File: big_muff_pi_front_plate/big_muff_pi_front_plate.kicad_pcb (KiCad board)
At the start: 2 copper layers, 80 x 100 mm, 13 parts, among them J1 top_panel_connector

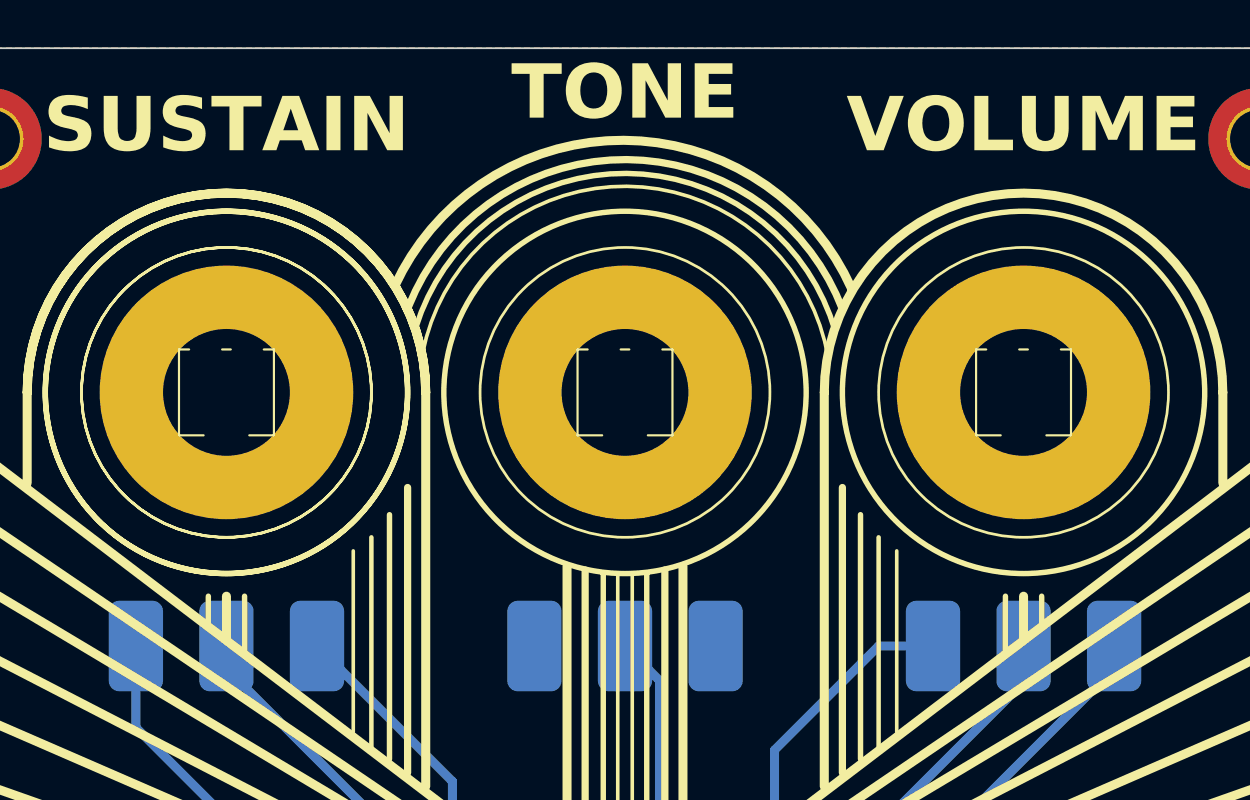
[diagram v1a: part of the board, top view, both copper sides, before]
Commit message: Pots rotated, more space for the battery.
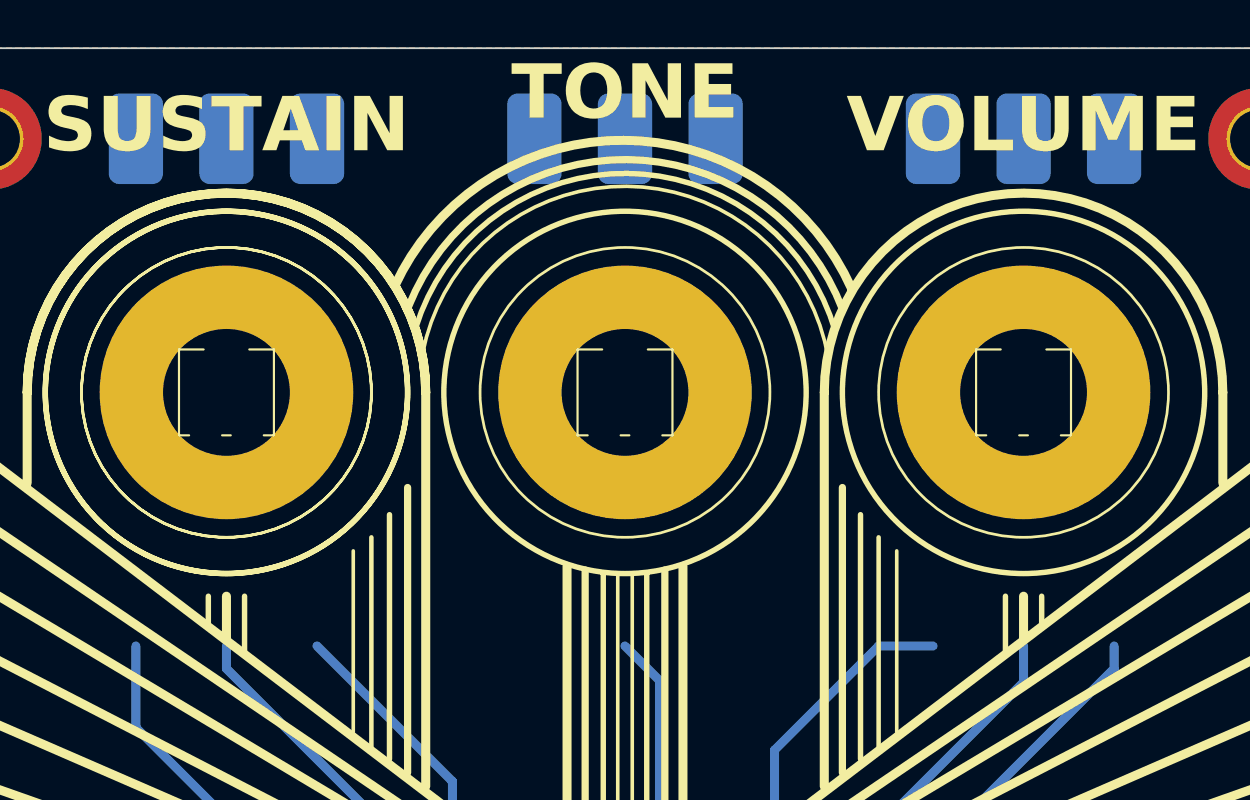
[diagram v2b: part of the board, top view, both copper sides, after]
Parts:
- turned RV1 to 180 degrees
- turned RV2 to 180 degrees
- turned RV3 to 180 degrees

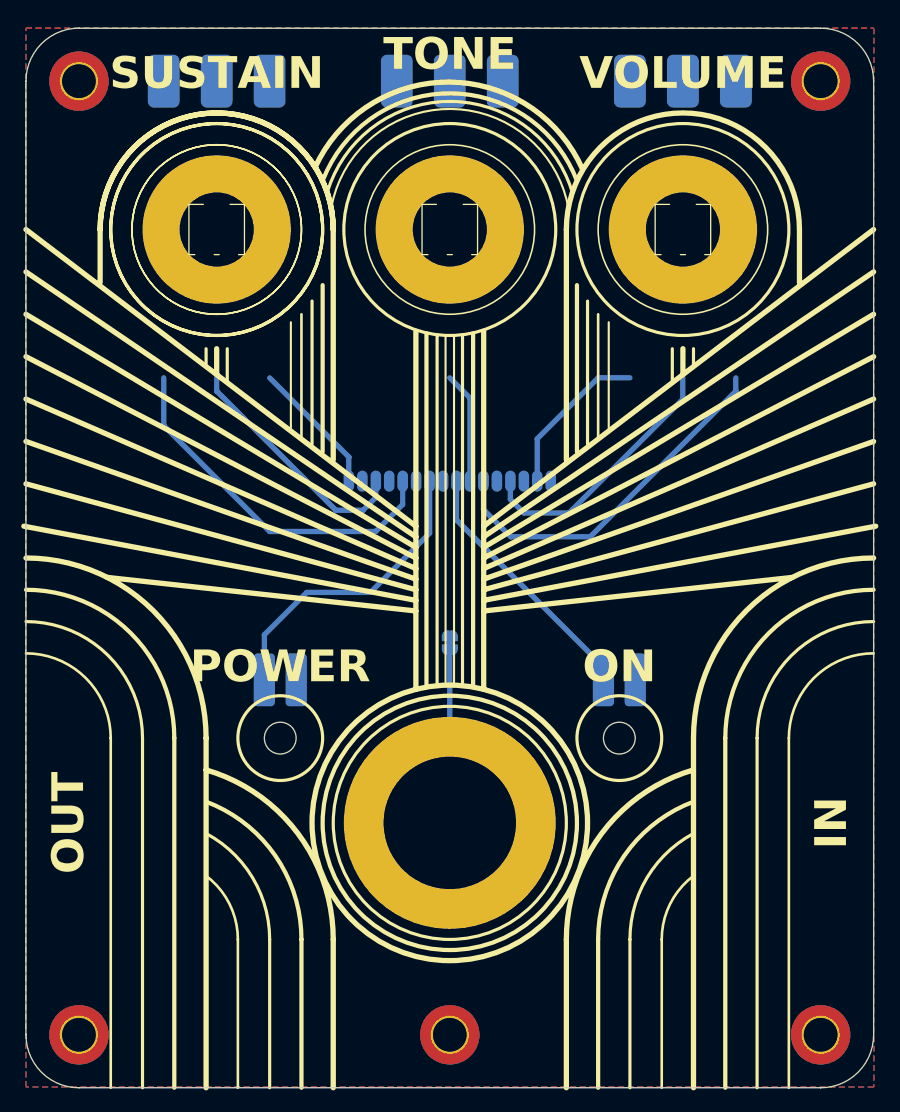
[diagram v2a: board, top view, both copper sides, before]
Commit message: Potentiometers checked, LED updated
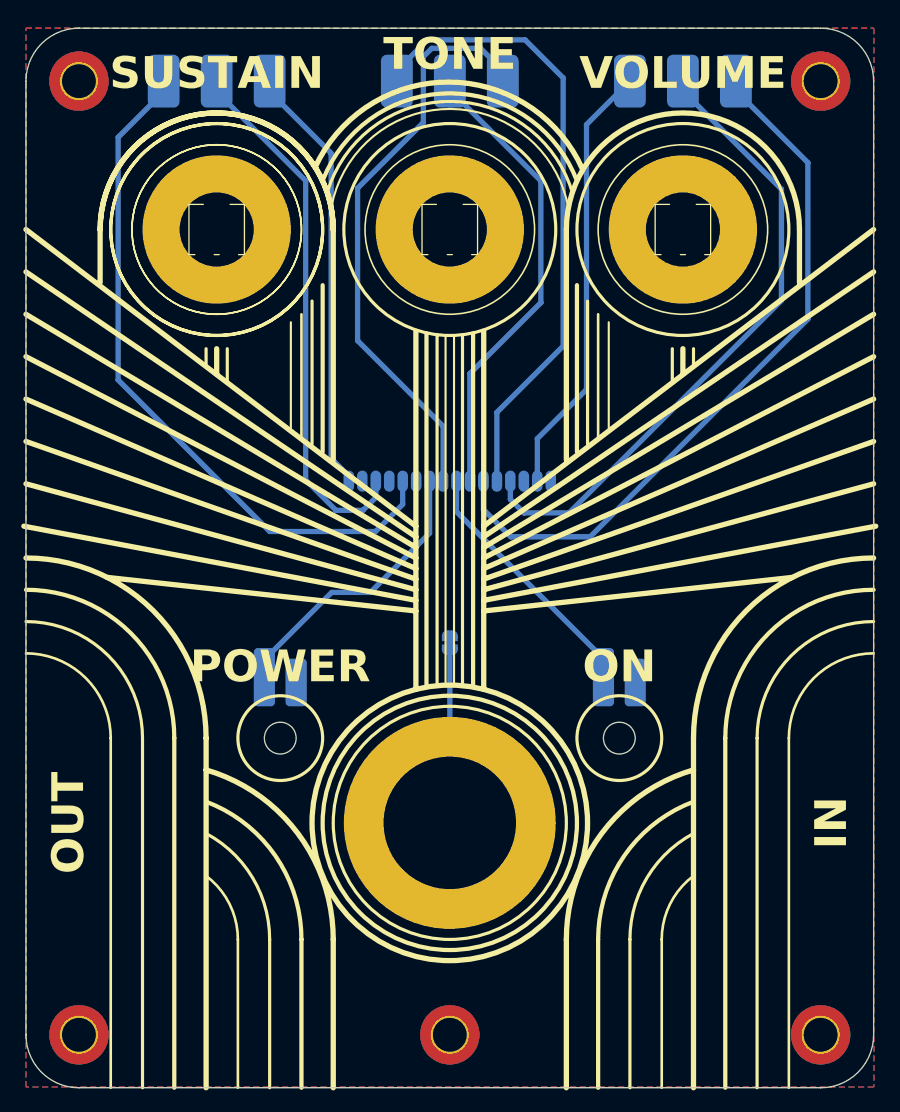
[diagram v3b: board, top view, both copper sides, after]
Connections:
- J1 pad 1: unconnected-(J1F-VCC-Pad1) -> 9V
- J1 pad 3: unconnected-(J1F-GND-Pad3) -> 0
- RV1 pad 1: Net-(J1A-Pin_2) -> Net-(J1A-Pin_6)
- RV1 pad 3: Net-(J1A-Pin_6) -> Net-(J1A-Pin_2)
- RV2 pad 1: Net-(J1B-Pin_5) -> Net-(J1B-Pin_9)
- RV2 pad 3: Net-(J1B-Pin_9) -> Net-(J1B-Pin_5)
- RV3 pad 1: Net-(J1C-Pin_12) -> Net-(J1C-Pin_16)
- RV3 pad 3: Net-(J1C-Pin_16) -> Net-(J1C-Pin_12)
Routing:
- net Net-(J1B-Pin_5): track 0.00 -> 60.0 mm
- net Net-(J1B-Pin_9): track 0.00 -> 55.7 mm
- net Net-(J1A-Pin_4): track 25.0 -> 60.7 mm
- net Net-(J1A-Pin_6): track 34.5 -> 68.1 mm
- net Net-(J1B-Pin_7): track 10.5 -> 44.1 mm
- net Net-(J1C-Pin_12): track 34.5 -> 66.0 mm
- net Net-(J1C-Pin_16): track 12.8 -> 40.8 mm
- net Net-(J1C-Pin_14): track 23.0 -> 51.0 mm
- net Net-(J1A-Pin_2): track 15.1 -> 41.4 mm
- net Net-(D2-A): track 28.7 -> 27.3 mm

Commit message: Front plate update.
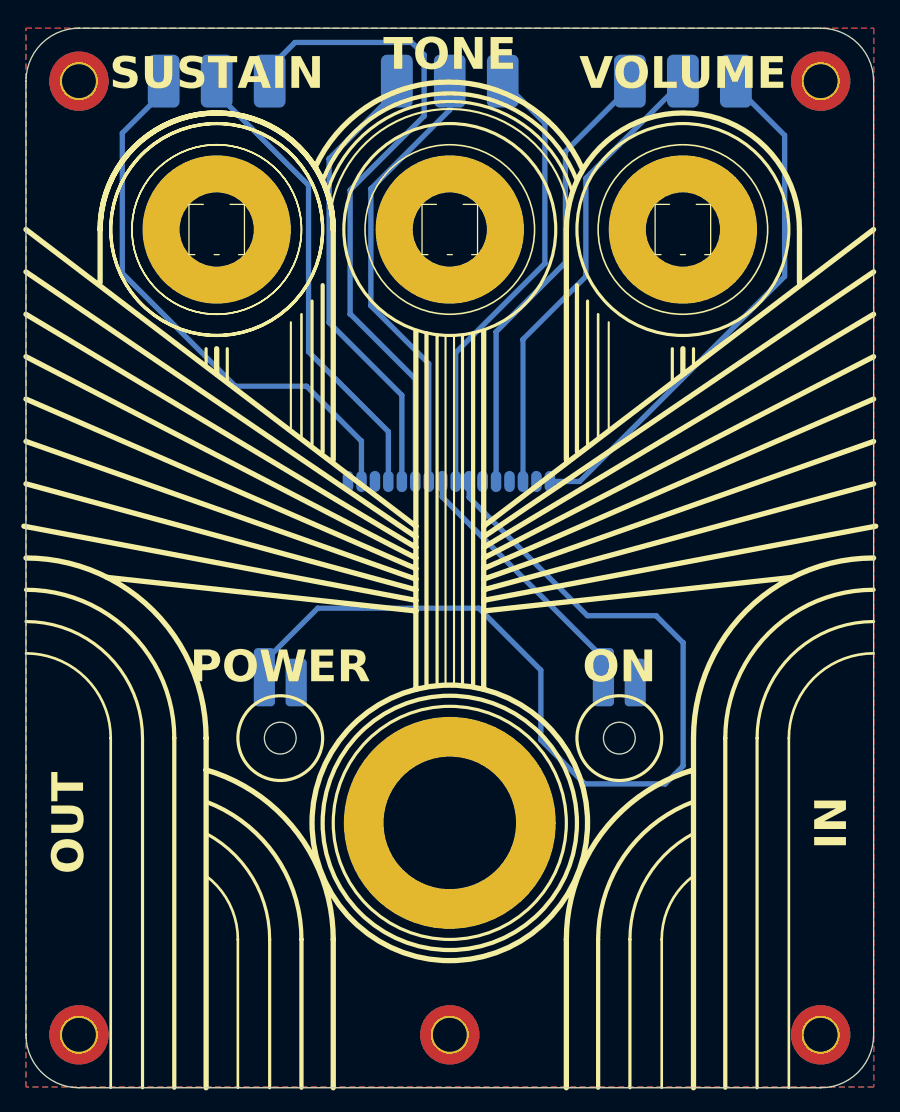
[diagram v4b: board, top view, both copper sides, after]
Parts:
- removed JP4: SolderJumper_2_Bridged, Jumper:SolderJumper-2_P1.3mm_Bridged_RoundedPad1.0x1.5mm
- H1, H11, H2, H3, H4: value MountingHole -> MountingHole_Pad
- RV1, RV2, RV3: value R_Potentiometer -> pot_gnd
- moved J1 19.1 mm to (80.4, 92.8), turned to -90 degrees
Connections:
- H1 pad 1: (no net) -> 0
- H11 pad 1: (no net) -> 0
- H2 pad 1: (no net) -> 0
- H3 pad 1: (no net) -> 0
- H4 pad 1: (no net) -> 0
- H8 pad 1: Net-(JP4-B) -> 0
- RV1 pad 1: Net-(J1A-Pin_6) -> Net-(J1C-Pin_16)
- RV1 pad 2: Net-(J1A-Pin_4) -> Net-(J1C-Pin_14)
- RV1 pad 3: Net-(J1A-Pin_2) -> Net-(J1C-Pin_12)
- RV3 pad 1: Net-(J1C-Pin_16) -> Net-(J1A-Pin_6)
- RV3 pad 2: Net-(J1C-Pin_14) -> Net-(J1A-Pin_4)
- RV3 pad 3: Net-(J1C-Pin_12) -> Net-(J1A-Pin_2)
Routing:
- net Net-(D2-A): track 27.3 -> 93.5 mm
- net Net-(J1C-Pin_12): track 66.0 -> 43.0 mm
- net Net-(J1B-Pin_5): track 60.0 -> 43.3 mm
- net Net-(JP4-B): track 16.3 -> 0.00 mm
- net Net-(J1A-Pin_4): track 60.7 -> 44.8 mm
- net Net-(J1B-Pin_9): track 55.7 -> 42.9 mm
- net Net-(J1A-Pin_2): track 41.4 -> 52.7 mm
- net Net-(J1C-Pin_16): track 40.8 -> 50.5 mm
- net Net-(J1C-Pin_14): track 51.0 -> 44.0 mm
- net Net-(J1A-Pin_6): track 68.1 -> 63.0 mm
- net Net-(J1B-Pin_7): track 44.1 -> 43.1 mm

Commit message: Big muff pi, new connector position.
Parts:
- J1: footprint pedale:bottom_connector -> Connector_IDC:IDC-Header_2x08_P2.54mm_Vertical
- moved J1 11.7 mm to (81.1, 81.1)

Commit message: Front plate update, componets created.
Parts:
- J1: footprint Connector_IDC:IDC-Header_2x08_P2.54mm_Vertical -> pedale:IDC-Header_2x08_faux_SMD

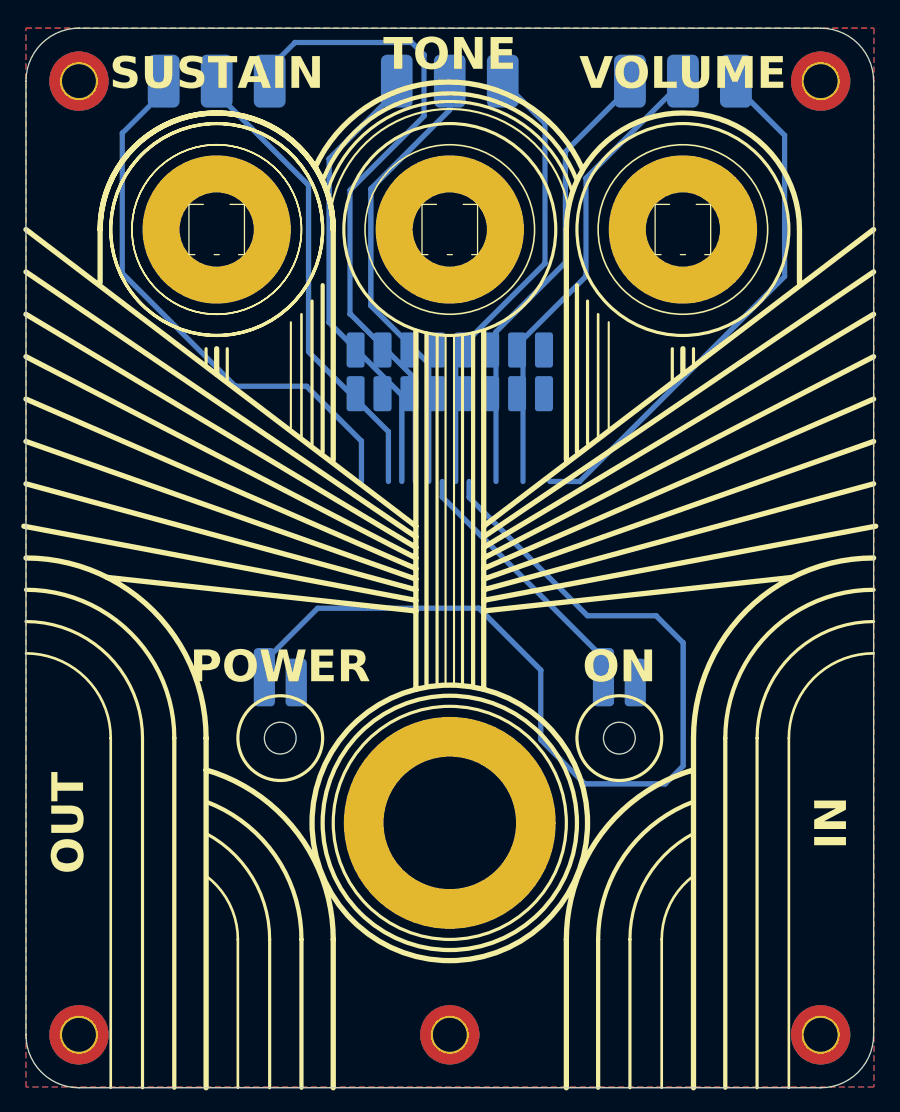
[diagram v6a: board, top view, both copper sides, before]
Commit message: Front plate trace done.
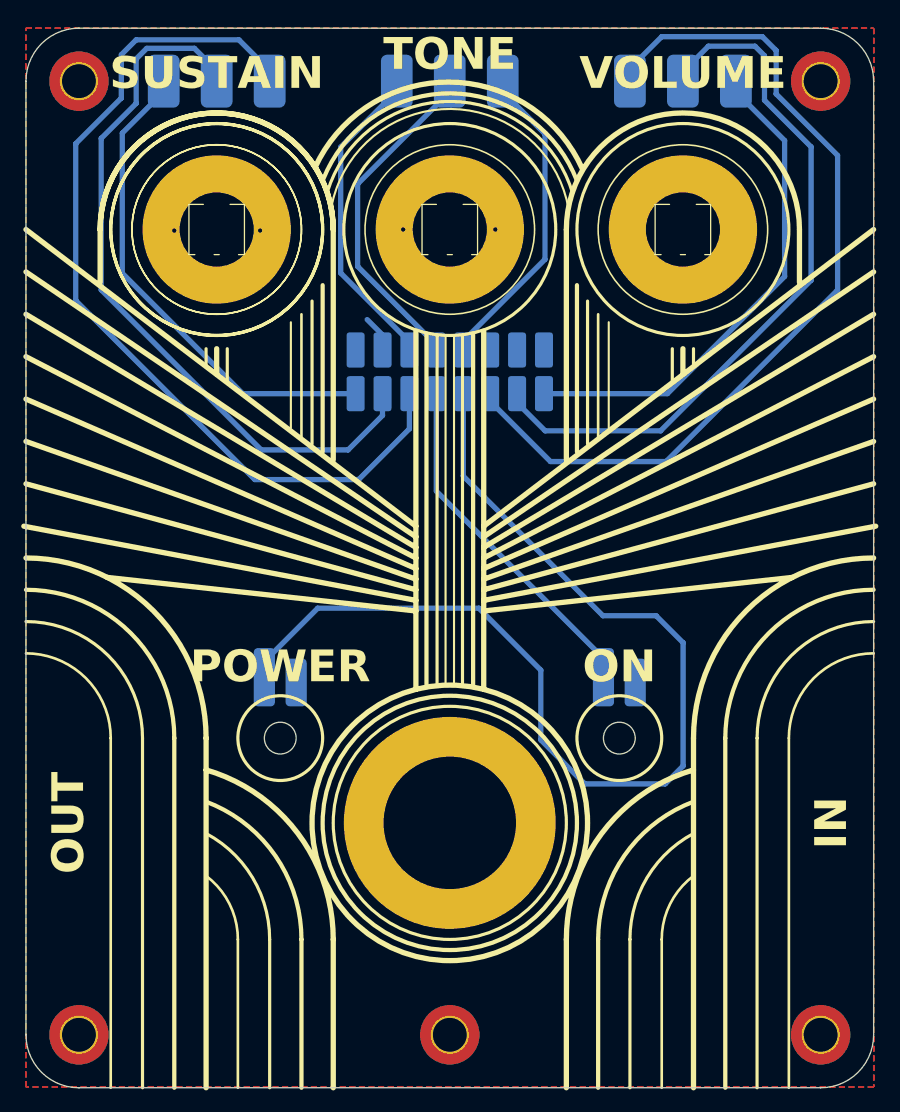
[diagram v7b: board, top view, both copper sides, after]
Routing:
- net Net-(J1C-Pin_12): track 43.0 -> 84.4 mm
- net Net-(J1C-Pin_14): track 44.0 -> 68.6 mm
- net Net-(J1A-Pin_4): track 44.8 -> 69.3 mm
- net Net-(J1A-Pin_6): track 63.0 -> 85.6 mm
- net Net-(J1B-Pin_5): track 43.3 -> 30.3 mm
- net Net-(J1B-Pin_9): track 42.9 -> 30.2 mm
- net Net-(J1B-Pin_7): track 43.1 -> 32.1 mm
- net Net-(D1-A): track 24.8 -> 33.3 mm
- net Net-(D2-A): track 93.5 -> 101.2 mm
- net Net-(J1A-Pin_2): track 52.7 -> 46.5 mm
- net 0: track 0.00 -> 3.47 mm, vias 0 -> 4
- net Net-(J1C-Pin_16): track 50.5 -> 47.6 mm

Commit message: Rounded traces za front plate.
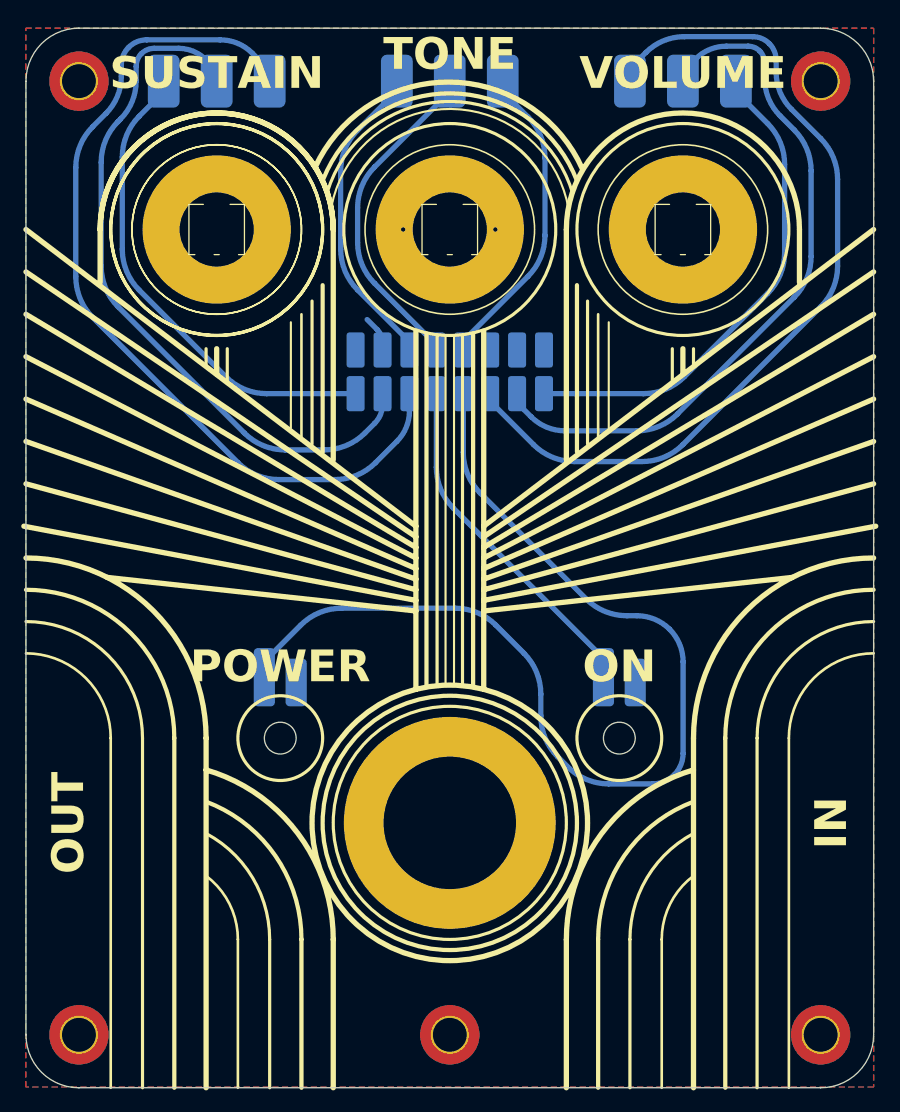
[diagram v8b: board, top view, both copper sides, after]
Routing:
- net Net-(D2-A): track 101.2 -> 98.6 mm
- net Net-(J1A-Pin_6): track 85.6 -> 83.6 mm
- net Net-(J1C-Pin_12): track 84.4 -> 82.5 mm
- net Net-(J1A-Pin_4): track 69.3 -> 67.5 mm
- net Net-(J1C-Pin_14): track 68.6 -> 66.9 mm
- net Net-(J1C-Pin_16): track 47.6 -> 46.8 mm
- net Net-(J1A-Pin_2): track 46.5 -> 45.6 mm
- net Net-(J1B-Pin_9): track 30.2 -> 29.6 mm
- net Net-(J1B-Pin_5): track 30.3 -> 29.6 mm
- net Net-(J1B-Pin_7): track 32.1 -> 31.4 mm
- net 0: track 3.47 -> 3.39 mm, vias 4 -> 2
